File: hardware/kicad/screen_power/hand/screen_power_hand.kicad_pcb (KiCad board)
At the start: 2 copper layers, 68 x 76 mm, 41 parts, among them J1 AUX 5V INPUT, J101 PI USB / XH4, J102 TOUCH / XH4, J103 SCREEN 1 POWER, J2 GPIO17 / GND, J201 PI USB / XH4, J202 TOUCH / XH4, J203 SCREEN 2 POWER, K101 IM02TS, K201 IM02TS, Q1 2N3904, Q101 2N7000, Q2 2N3906, Q201 2N7000, Q3 SUP70101EL, Q4 SUP70101EL

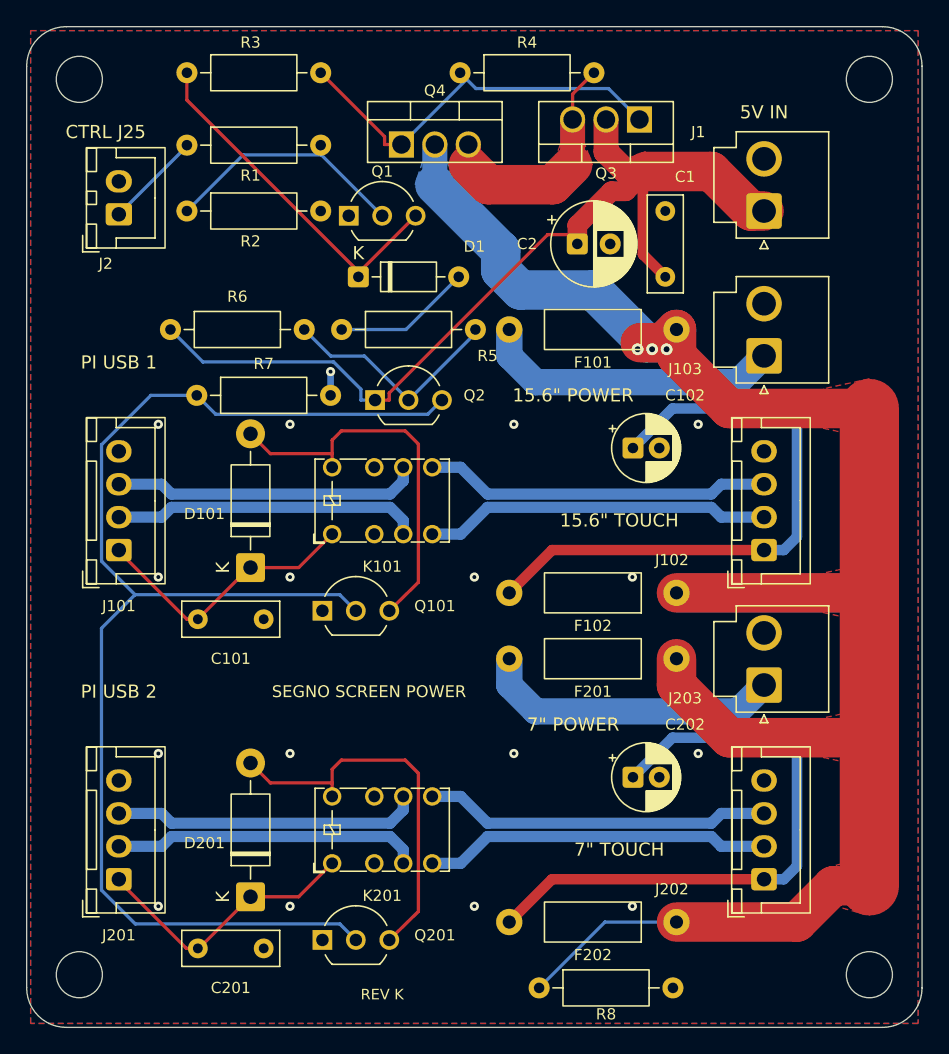
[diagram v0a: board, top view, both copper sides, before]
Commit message: chore(hardware): sync the CAD tree from the published screen-power branch
Takes hardware/kicad wholesale from codex/screen-power-board-1072 at
2b45a6a, so this branch carries the root session's validations, guards,
schematics, models and the three current native boards - including the
applied AUX input finish - before any further routing or placement work.
The one-time AUX patch script goes with it: it has been applied there.

Co-Authored-By: Claude Opus 5 (1M context) <noreply@anthropic.com>
Claude-Session: https://claude.ai/code/session_01XRHQAKB7tDQYJu6Fmz1NXv
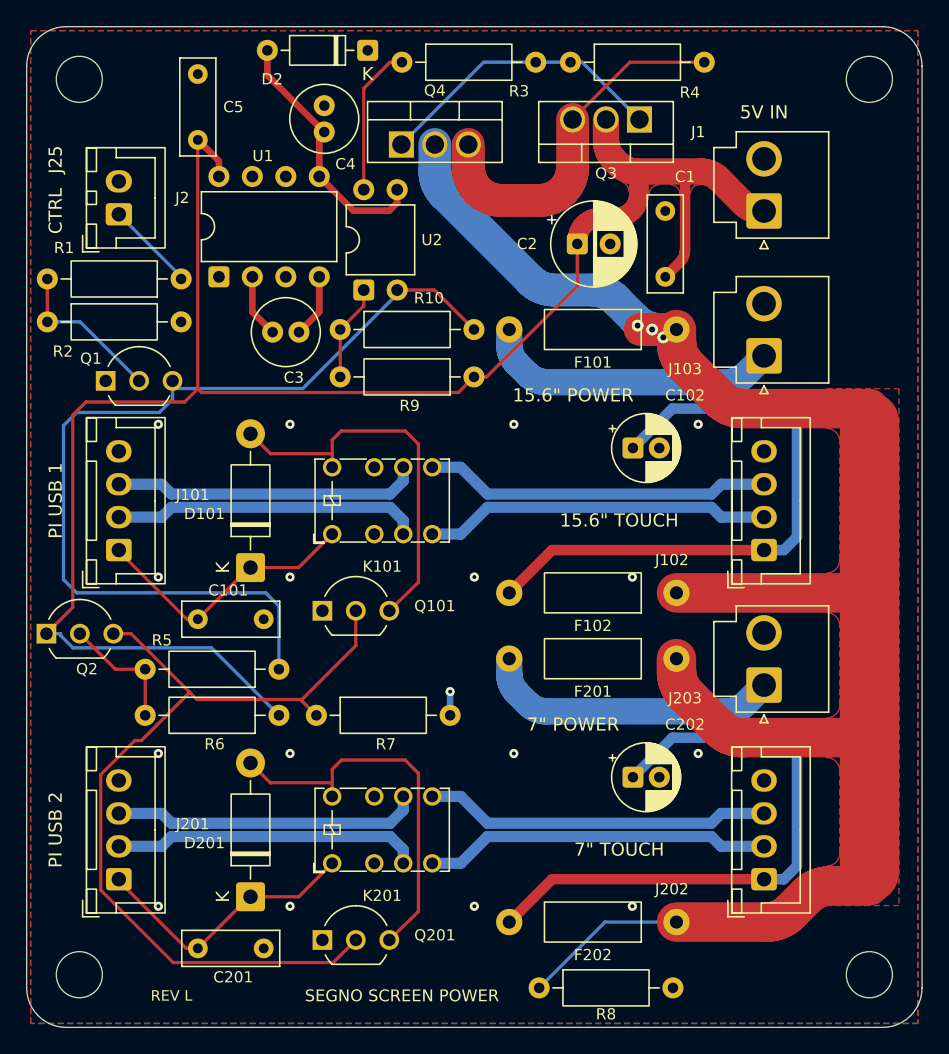
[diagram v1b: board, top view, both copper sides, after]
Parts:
- removed D1: 1N4148, D_DO-35_SOD27_P7.62mm_Horizontal
- added C3: 10uF 25V bipolar, C_Radial_D5.0mm_H11.0mm_P2.00mm, F.Cu at (18.7, 23.2)
- added C4: 10uF 25V bipolar, C_Radial_D5.0mm_H11.0mm_P2.00mm, F.Cu at (22.6, 6.00)
- added C5: 100nF 63V, C_Rect_L7.2mm_W2.5mm_P5.00mm, F.Cu at (13.0, 8.60)
- added D2: BAT85S, D_DO-35_SOD27_P7.62mm_Horizontal, F.Cu at (25.9, 1.80)
- added R10: 10k 1%, R_Axial_DIN0207_L6.3mm_D2.5mm_P10.16mm_Horizontal, F.Cu at (23.8, 23.0)
- added R9: 2.4k 1%, R_Axial_DIN0207_L6.3mm_D2.5mm_P10.16mm_Horizontal, F.Cu at (34.0, 26.6)
- added U1: LMC7660IN, DIP-8_W7.62mm, F.Cu at (14.6, 19.0)
- added U2: TLP627M, DIP-4_W7.62mm, F.Cu at (25.6, 20.0)
- Q101, Q201: value 2N7000 -> TN0702
- R4: value 330k 1% -> 22k 1%
- moved Q2 30.6 mm to (1.50, 46.1)
- moved R6 30.4 mm to (19.2, 52.3), turned to 180 degrees
- moved R5 26.2 mm to (19.2, 48.8), turned to 180 degrees
- moved R7 25.9 mm to (22.0, 52.3)
- moved Q1 22.3 mm to (6.00, 26.9)
- moved R3 16.3 mm to (28.5, 2.70)
- moved R2 13.5 mm to (1.57, 22.4)
- moved R1 10.2 mm to (11.7, 19.2), turned to 180 degrees
- moved R4 8.42 mm to (41.3, 2.70)
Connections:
- R3 pad 1: CONTROL_SINK -> GATE_SINK
- R5 pad 1: BUFFER_SINK -> CONTROL_SINK
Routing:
- net AUX_5V: track 72.5 -> 139.1 mm
- net CONTROL_SINK: track 27.0 -> 71.6 mm
- net DATA_ENABLE: track 102.5 -> 67.0 mm
- net NEG_5V: track 0.00 -> 19.8 mm
- net GATE_SINK: track 0.00 -> 11.4 mm
- net BUFFER_SINK: track 10.5 -> 0.00 mm
- net COMMON_SOURCE: track 18.4 -> 28.0 mm
- net POWER_GATE: track 30.8 -> 22.5 mm
- net BUFFER_BASE: track 17.6 -> 9.58 mm
- net GATE_LED: track 0.00 -> 7.34 mm
- net CONTROL_BASE: track 19.2 -> 12.1 mm
- net SWITCHED_5V: track 148.6 -> 142.3 mm
- net PUMP_CAP_PLUS: track 0.00 -> 4.84 mm
- net PUMP_CAP_MINUS: track 0.00 -> 4.84 mm
- net PI_GPIO17: track 7.39 -> 6.87 mm
- removed copper zone on F.Cu, net COMMON_SOURCE
- removed copper zone on B.Cu, net SWITCHED_5V
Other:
- board text added: "CTRL"
- board text added: "J25"
- board text added: "REV L"
- board text added: "SEGNO SCREEN POWER / REV L"
- board text removed: "CTRL J25"
- board text removed: "REV K"
- board text removed: "SEGNO SCREEN POWER / REV K"
